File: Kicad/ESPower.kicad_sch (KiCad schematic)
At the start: 36 parts, among them J1 Input, J2 Power Switch, J3 Output, J4 Battery, J5 GPIO, Q1 DMP2035U-7, Q2 FS8205A, SW1 PowerPath enable, SW2 A, SW3 B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

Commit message: Improved schematic
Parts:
- removed C3: 10µF, Capacitor_Tantalum_SMD:CP_EIA-3216-10_Kemet-I, symbol ESPower-rescue:CP-Device
- added C3, C8: 10uF, Capacitor_SMD:C_0603_1608Metric, symbol Device:C
- added R11: 10k, Resistor_SMD:R_0603_1608Metric, symbol Device:R
- C1: value 220µF -> 220uF; footprint Capacitor_THT:CP_Radial_D6.3mm_P2.50mm -> Capacitor_Tantalum_SMD:CP_EIA-6032-28_Kemet-C; LCSC (none) -> C123271
- C5: value 10µF -> 10uF
- C7: value 470µF -> 220uF; footprint Capacitor_THT:CP_Radial_D8.0mm_P3.50mm -> Capacitor_Tantalum_SMD:CP_EIA-6032-28_Kemet-C; LCSC (none) -> C123271
- Q2: MANUFACTURER Fortune Semiconductor -> (none); MAXIMUM_PACKAGE_HEIGHT 1.2mm -> (none); PARTREV 1.7 -> (none); STANDARD IPC 7351B -> (none)
- R1, R9: value 100kΩ -> 100k
- R10: value 12kΩ -> 10k; LCSC C22790 -> C25804
- R2, R3, R4: value 1kΩ -> 1k
- R5: value 2.4kΩ -> 2.4k
- R6, R7: value 1.2kΩ -> 1.2k
- R8: value 100Ω -> 100
- SW1, SW2, SW3: footprint Resistor_SMD:R_0805_2012Metric -> Jumper:SolderJumper-2_P1.3mm_Open_TrianglePad1.0x1.5mm
- U1: MANUFACTURER NanJing Top Power ASIC Corp. -> (none); MAXIMUM_PACKAGE_HEIGHT 1.75mm -> (none); STANDARD IPC 7351B -> (none)
- U2: MPN DW01A -> (none); VALUE DW01A -> (none)
- U5: MANUFACTURER AI-Thinker -> (none); MAXIMUM_PACKAGE_HEIGHT 11.2 mm -> (none); PARTREV V1.2 -> (none); STANDARD Manufacturer recommendations or IPC 7351B -> (none)
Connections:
- net +3V3: now also C3.1, R11.1
- net +5V: now also C8.1
- net GND: now also C3.2, C8.2
- net at J5.1 (Pin_1), U5.3 (IO0): now also R11.2
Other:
- note removed: "C1 plus petit ?"
- note removed: "C3 tantale ou non polasisé ? chez datacheet"
- note removed: "C7 100µF ? Difference aluminium/tantal ?"
- moved on the sheet: C6, C7, J5, R10, R9, U4, U5

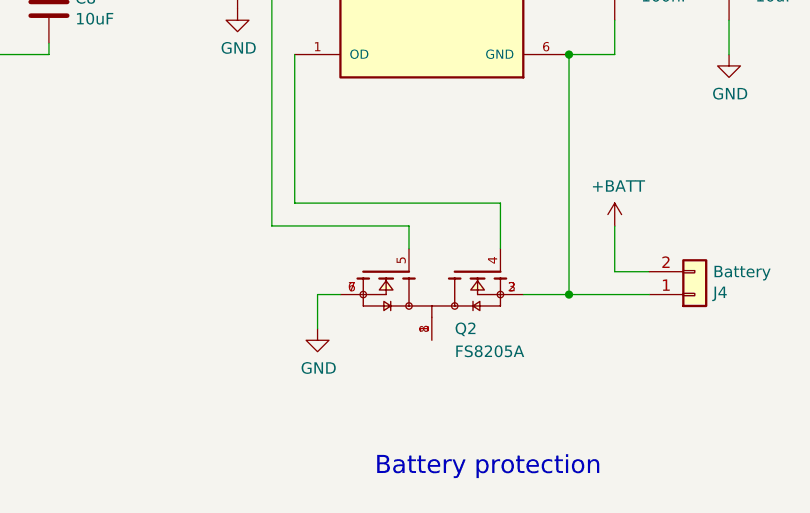
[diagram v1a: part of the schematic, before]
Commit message: Switched Q2 footprint
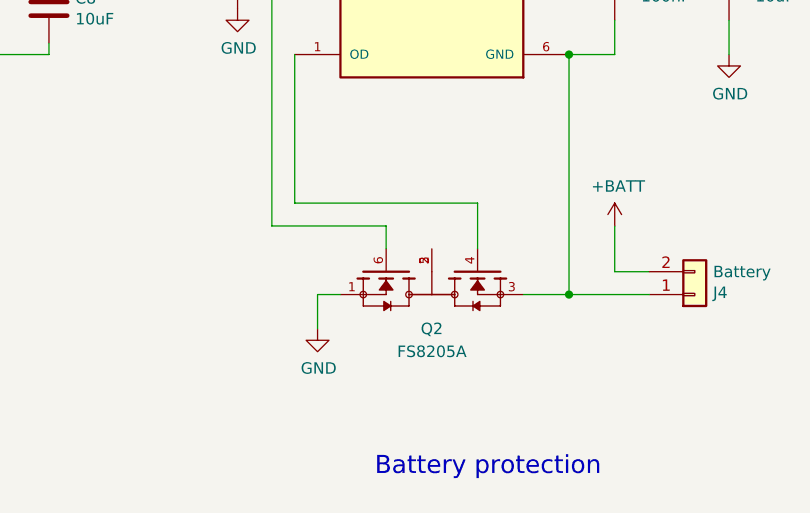
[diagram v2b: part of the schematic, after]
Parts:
- removed Q2: FS8205A, Package_SO:TSSOP-8_4.4x3mm_P0.65mm, symbol FS8205A:FS8205A
- added Q2: FS8205A, Package_TO_SOT_SMD:SOT-23-6, symbol FS8205:FS8205
- D3: LCSC C72041 -> C2288
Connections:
- net GND: now also Q2.1
- net at U2.1 (OD): now also Q2.4
- net at U2.3 (OC): now also Q2.6
- net at C4.2, J4.1 (Pin_1), U2.6 (GND): now also Q2.3
- new net: Q2.2, Q2.5
